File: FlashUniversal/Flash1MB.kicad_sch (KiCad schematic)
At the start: 26 parts, among them J1 Conn_02x04_Odd_Even, J10 Conn_01x01_Pin, J11 Conn_01x01_Pin, J12 Conn_01x01_Pin, J13 Conn_01x01_Pin, J14 Conn_01x01_Pin, J15 Conn_01x01_Pin, J16 Conn_01x01_Pin, J17 Conn_01x01_Pin, J18 Conn_01x01_Pin, J19 Conn_01x01_Pin, J2 Conn_01x01_Pin, J20 Conn_01x01_Pin, J21 Conn_01x01_Pin, J22 Conn_01x01_Pin, J3 Conn_01x01_Pin, J4 Conn_01x01_Pin, J5 Conn_01x01_Pin, J6 Conn_01x01_Pin, J7 Conn_01x01_Pin, J8 Conn_01x01_Pin, J9 Conn_01x01_Pin

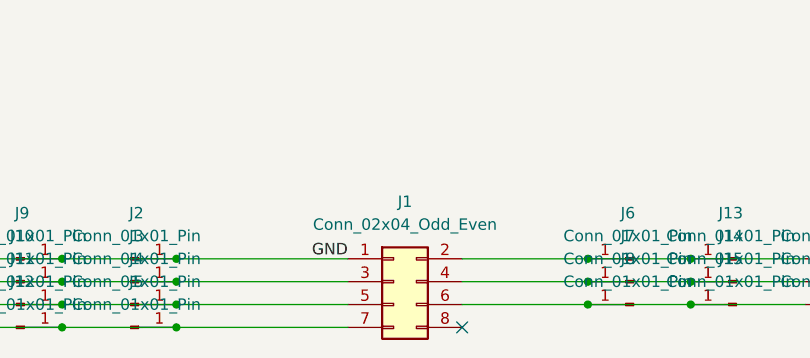
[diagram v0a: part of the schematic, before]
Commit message: DB und flasher korrektur
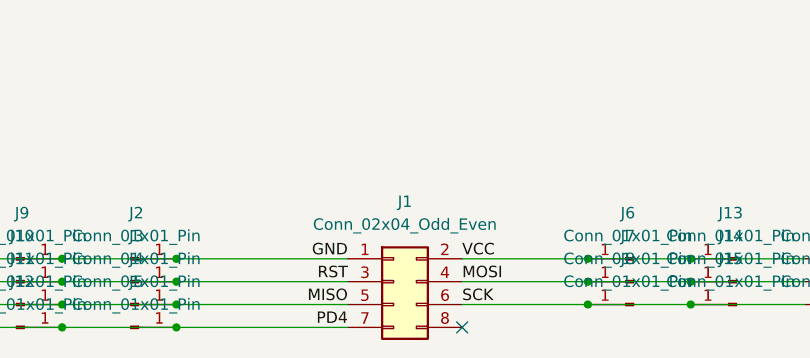
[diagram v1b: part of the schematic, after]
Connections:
- net MOSI: now reaches J1.4 (Pin_4), J14.1 (Pin_1), J21.1 (Pin_1), J7.1 (Pin_1)
- net RST: now reaches J1.3 (Pin_3), J10.1 (Pin_1), J17.1 (Pin_1), J3.1 (Pin_1)
- net MISO: now reaches J1.5 (Pin_5), J11.1 (Pin_1), J18.1 (Pin_1), J4.1 (Pin_1)
- net SCK: now reaches J1.6 (Pin_6), J15.1 (Pin_1), J22.1 (Pin_1), J8.1 (Pin_1)
- net VCC: now reaches J1.2 (Pin_2), J13.1 (Pin_1), J20.1 (Pin_1), J6.1 (Pin_1)
- net PD4: now reaches J1.7 (Pin_7), J12.1 (Pin_1), J19.1 (Pin_1), J5.1 (Pin_1)
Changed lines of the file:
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@@
+		)
+	)
+	(label "VCC"
+		(at 129.54 50.8 0)
+		(fields_autoplaced yes)
+		(effects
+			(font
+				(size 1.27 1.27)
+			)
+			(justify left bottom)
 		)
 	)
 	(label "GND"
 		(at 116.84 50.8 180)
+		(fields_autoplaced yes)
+		(effects
+			(font
+				(size 1.27 1.27)
+			)
+			(justify right bottom)
+		)
+	)
+	(label "PD4"
+		(at 116.84 58.42 180)
+		(fields_autoplaced yes)
+		(effects
+			(font
+				(size 1.27 1.27)
+			)
+			(justify right bottom)
+		)
+	)
+	(label "MISO"
+		(at 116.84 55.88 180)
 		(fields_autoplaced yes)
 		(effects
@@
 		)
 	)
+	(label "MOSI"
+		(at 129.54 53.34 0)
+		(fields_autoplaced yes)
+		(effects
+			(font
+				(size 1.27 1.27)
+			)
+			(justify left bottom)
+		)
+	)
+	(label "SCK"
+		(at 129.54 55.88 0)
+		(fields_autoplaced yes)
+		(effects
+			(font
+				(size 1.27 1.27)
+			)
+			(justify left bottom)
+		)
+	)
 	(label "GND"
 		(at 20.32 52.07 180)
 		(fields_autoplaced yes)
 		(effects
+			(font
+				(size 1.27 1.27)
+			)
+			(justify right bottom)
+		)
+	)
+	(label "RST"
+		(at 116.84 53.34 180)
+		(fields_autoplaced yes)
+		(effects

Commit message: kicad 9 update
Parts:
- added H5, H6: MountingHole_Pad, MountingHole:MountingHole_2.2mm_M2_DIN965_Pad, symbol Mechanical:MountingHole_Pad
- added J23, J24, J25, J26, J27, J28, J29: Conn_01x01_Pin, Connector_PinHeader_2.54mm:PinHeader_1x01_P2.54mm_Vertical, symbol Connector:Conn_01x01_Pin
- added J30: Conn_02x03_Odd_Even, Connector_PinHeader_2.54mm:PinHeader_2x03_P2.54mm_Vertical, symbol Connector_Generic:Conn_02x03_Odd_Even
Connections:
- net GND: now also H5.1, H6.1, J26.1 (Pin_1), J30.6 (Pin_6)
- net MISO: now also J28.1 (Pin_1), J30.1 (Pin_1)
- net MOSI: now also J24.1 (Pin_1), J30.4 (Pin_4)
- net PD4: now also J29.1 (Pin_1)
- net RST: now also J27.1 (Pin_1), J30.5 (Pin_5)
- net SCK: now also J25.1 (Pin_1), J30.3 (Pin_3)
- net VCC: now also J23.1 (Pin_1), J30.2 (Pin_2)
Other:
- moved on the sheet: J12, J13, J19, J20, J7

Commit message: loch
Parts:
- H1, H2, H3, H4: footprint MountingHole:MountingHole_4mm_Pad -> MountingHole:MountingHole_4.3mm_M4_DIN965_Pad
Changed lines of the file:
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@@
 			)
 		)
-		(property "Footprint" "MountingHole:MountingHole_4mm_Pad"
+		(property "Footprint" "MountingHole:MountingHole_4.3mm_M4_DIN965_Pad"
 			(at 20.32 49.53 0)
 			(effects
@@
 			)
 		)
-		(property "Footprint" "MountingHole:MountingHole_4mm_Pad"
+		(property "Footprint" "MountingHole:MountingHole_4.3mm_M4_DIN965_Pad"
 			(at 20.32 31.75 0)
 			(effects
@@
 			)
 		)
-		(property "Footprint" "MountingHole:MountingHole_4mm_Pad"
+		(property "Footprint" "MountingHole:MountingHole_4.3mm_M4_DIN965_Pad"
 			(at 20.32 40.64 0)
 			(effects
@@
 			)
 		)
-		(property "Footprint" "MountingHole:MountingHole_4mm_Pad"
+		(property "Footprint" "MountingHole:MountingHole_4.3mm_M4_DIN965_Pad"
 			(at 20.32 22.86 0)
 			(effects
